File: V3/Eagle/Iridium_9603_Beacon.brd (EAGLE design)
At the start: 50.8 x 71.1 mm, 64 parts, among them J1 SS4-10-3.50-X-D, Q1 DMG3415U-7, U1 MCP111T-195I/TT, U2 SPX3819-3.3, U3 LTC3225EDDB#TRMPBF, U4 MPL3115A2LGA8, U5 ATSAMD21G18_QFN, U6 SAM-M8Q, X1 32.768

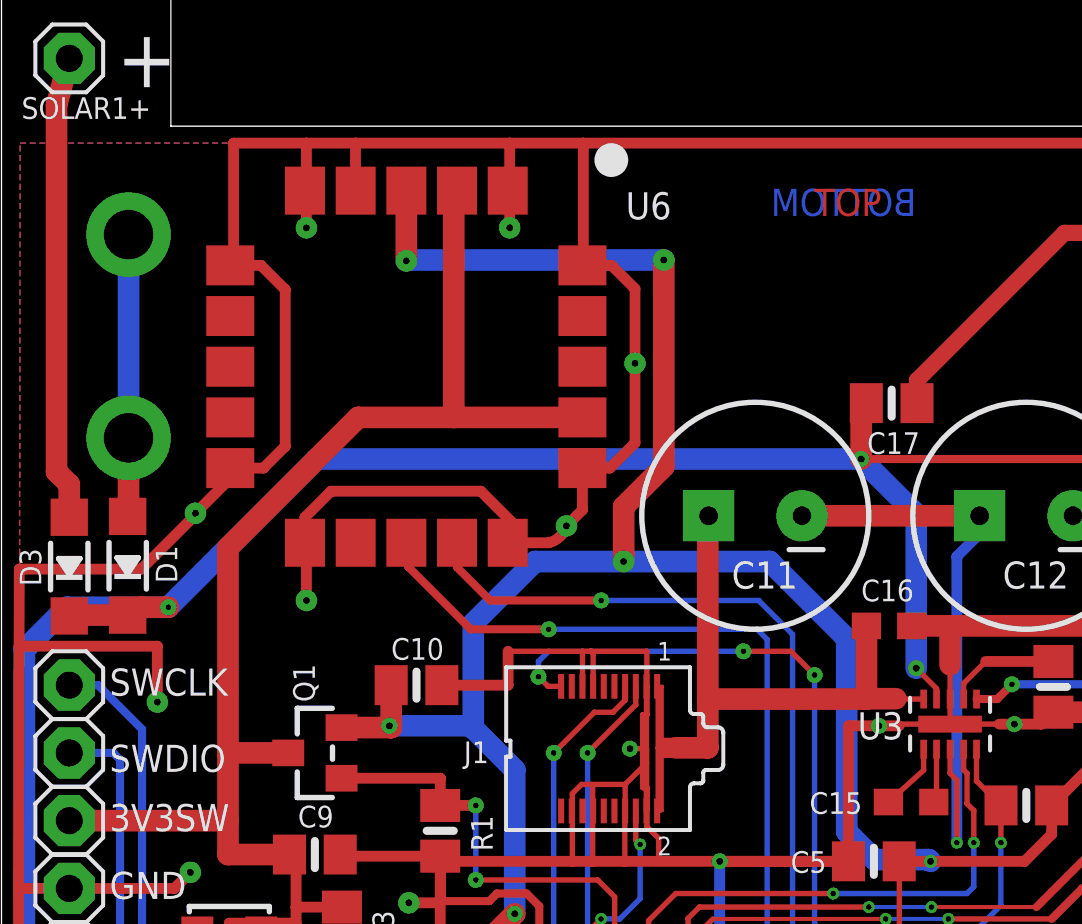
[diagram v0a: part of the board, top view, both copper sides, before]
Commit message: Improved the ground plane under the SAM-M8Q
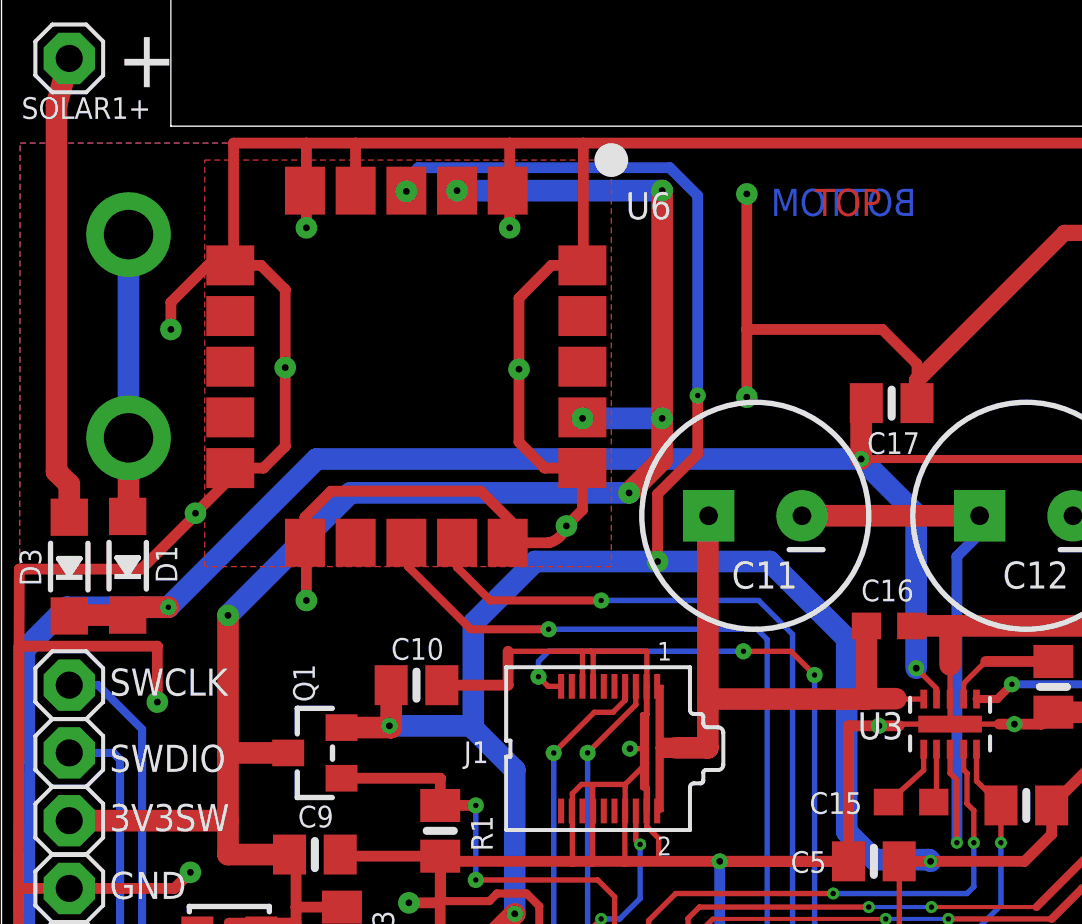
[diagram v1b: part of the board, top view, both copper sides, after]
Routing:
- net GND: track 606.7 -> 627.1 mm, vias 18 -> 22
- net 3V3SW: track 58.0 -> 71.1 mm, vias 0 -> 6
- net +3V3: track 174.7 -> 176.8 mm
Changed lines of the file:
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@@
 <text x="30.48" y="62.6745" size="1.016" layer="1" font="vector" ratio="16">TOP</text>
 <text x="34.29" y="62.6745" size="1.016" layer="16" font="vector" ratio="16" rot="MR0">BOTTOM</text>
-<text x="25.3365" y="55.4355" size="1.4224" layer="22" ratio="18" rot="MR0" align="bottom-center">Please return to:
+<text x="25.62225" y="57.24525" size="1.4224" layer="22" ratio="18" rot="MR0" align="bottom-center">Please return to:
 Durham University
 ph-cfai-bit@durham.ac.uk</text>
@@
 <vertex x="50.2285" y="5.715"/>
 </polygon>
-<polygon width="0.4064" layer="1" spacing="0.8128" pour="hatch" isolate="0.4064">
+<polygon width="0.4064" layer="1" spacing="0.8128" pour="hatch" isolate="0.4064" rank="2">
 <vertex x="0.635" y="5.715"/>
 <vertex x="0.6985" y="65.405"/>
@@
 <wire x1="21.7765" y1="60.823" x2="21.81225" y2="60.85875" width="0.4064" layer="1"/>
 <wire x1="21.81225" y1="60.85875" x2="21.81225" y2="65.405" width="0.4064" layer="1"/>
-<wire x1="21.7765" y1="53.223" x2="22.8065" y2="53.223" width="0.4064" layer="1"/>
-<wire x1="22.8065" y1="53.223" x2="23.749" y2="54.1655" width="0.4064" layer="1"/>
-<wire x1="23.749" y1="59.944" x2="22.87" y2="60.823" width="0.4064" layer="1"/>
-<wire x1="22.87" y1="60.823" x2="21.7765" y2="60.823" width="0.4064" layer="1"/>
+<wire x1="21.7765" y1="53.223" x2="20.36175" y2="53.223" width="0.4064" layer="1"/>
+<wire x1="20.36175" y1="53.223" x2="19.39925" y2="54.19725" width="0.4064" layer="1"/>
+<wire x1="19.39925" y1="59.59475" x2="20.61575" y2="60.823" width="0.4064" layer="1"/>
+<wire x1="20.61575" y1="60.823" x2="21.7765" y2="60.823" width="0.4064" layer="1"/>
 <wire x1="18.9765" y1="50.423" x2="19.4945" y2="50.423" width="0.4064" layer="1"/>
 <wire x1="19.4945" y1="50.423" x2="20.5145" y2="50.423" width="0.4064" layer="1"/>
@@
 <wire x1="7.08025" y1="38.06825" x2="6.477" y2="37.465" width="0.4064" layer="1"/>
 <wire x1="6.477" y1="37.465" x2="2.54" y2="37.465" width="0.4064" layer="1"/>
-<via x="23.749" y="57.15" extent="1-16" drill="0.254" diameter="0.8128"/>
+<via x="19.39925" y="56.92775" extent="1-16" drill="0.254" diameter="0.8128"/>
 <via x="21.17725" y="51.054" extent="1-16" drill="0.254" diameter="0.8128"/>
 <via x="19.33575" y="21.9075" extent="1-16" drill="0.254" diameter="0.8128"/>
 <wire x1="20.5145" y1="50.423" x2="21.17725" y2="51.054" width="0.4064" layer="1" curve="60"/>
 <wire x1="21.7765" y1="51.65325" x2="21.17725" y2="51.054" width="0.4064" layer="1"/>
-<wire x1="23.749" y1="54.1655" x2="23.749" y2="57.15" width="0.4064" layer="1"/>
-<wire x1="23.749" y1="59.944" x2="23.749" y2="57.15" width="0.4064" layer="1"/>
+<wire x1="19.39925" y1="54.19725" x2="19.39925" y2="56.92775" width="0.4064" layer="1"/>
+<wire x1="19.39925" y1="59.59475" x2="19.39925" y2="56.92775" width="0.4064" layer="1"/>
 <via x="7.27075" y="51.53025" extent="1-16" drill="0.254" diameter="0.8128"/>
 <wire x1="7.27075" y1="51.53025" x2="8.5765" y2="52.836" width="0.4064" layer="1"/>
@@
 <wire x1="39.850059375" y1="62.0395" x2="34.31925" y2="56.508690625" width="0.6096" layer="1"/>
 <wire x1="34.31925" y1="56.508690625" x2="34.31925" y2="55.65775" width="0.6096" layer="1"/>
+<via x="10.63625" y="56.99125" extent="1-16" drill="0.254" diameter="0.8128"/>
+<polygon width="0.4064" layer="1" isolate="0.254">
+<vertex x="7.62" y="64.77"/>
+<vertex x="22.86" y="64.77"/>
+<vertex x="22.86" y="49.53"/>
+<vertex x="7.62" y="49.53"/>
+</polygon>
+<via x="27.94" y="55.88" extent="1-16" drill="0.254" diameter="0.8128"/>
+<via x="27.94" y="63.5" extent="1-16" drill="0.254" diameter="0.8128"/>
+<wire x1="27.94" y1="63.5" x2="27.94" y2="58.42" width="0.4064" layer="1"/>
+<wire x1="27.94" y1="58.42" x2="27.94" y2="55.88" width="0.4064" layer="1"/>
+<wire x1="34.31925" y1="55.65775" x2="34.31925" y2="57.12075" width="0.4064" layer="1"/>
+<wire x1="34.31925" y1="57.12075" x2="33.02" y2="58.42" width="0.4064" layer="1"/>
+<wire x1="33.02" y1="58.42" x2="27.94" y2="58.42" width="0.4064" layer="1"/>
+<via x="6.35" y="58.42" extent="1-16" drill="0.254" diameter="0.8128"/>
+<wire x1="8.5765" y1="60.823" x2="7.737" y2="60.823" width="0.4064" layer="1"/>
+<wire x1="7.737" y1="60.823" x2="6.35" y2="59.436" width="0.4064" layer="1"/>
+<wire x1="6.35" y1="59.436" x2="6.35" y2="58.42" width="0.4064" layer="1"/>
 </signal>
 <signal name="VBAT">
@@
 <wire x1="17.68475" y1="43.52925" x2="17.68475" y2="47.40275" width="0.8128" layer="16"/>
 <wire x1="17.68475" y1="47.40275" x2="20.0025" y2="49.7205" width="0.8128" layer="16"/>
-<wire x1="20.0025" y1="49.7205" x2="23.3236" y2="49.7205" width="0.8128" layer="16"/>
-<wire x1="23.3236" y1="49.7205" x2="28.79725" y2="49.7205" width="0.8128" layer="16"/>
+<wire x1="20.0025" y1="49.7205" x2="24.5936" y2="49.7205" width="0.8128" layer="16"/>
+<wire x1="24.5936" y1="49.7205" x2="28.79725" y2="49.7205" width="0.8128" layer="16"/>
 <wire x1="28.79725" y1="49.7205" x2="31.6865" y2="46.83125" width="0.8128" layer="16"/>
 <wire x1="31.6865" y1="46.83125" x2="31.6865" y2="39.59225" width="0.8128" layer="16"/>
@@
 <wire x1="21.36775" y1="23.71725" x2="23.2156" y2="21.8694" width="0.4064" layer="1"/>
 <wire x1="23.2156" y1="21.8694" x2="27.051" y2="21.8694" width="0.4064" layer="1"/>
-<via x="23.3236" y="49.7205" extent="1-16" drill="0.254" diameter="0.8128"/>
-<wire x1="23.3236" y1="49.7205" x2="23.3236" y2="51.7716" width="0.8128" layer="1"/>
-<wire x1="23.3236" y1="51.7716" x2="24.8285" y2="53.2765" width="0.8128" layer="1"/>
-<wire x1="24.8285" y1="53.2765" x2="24.8285" y2="61.0235" width="0.8128" layer="1"/>
-<via x="24.8285" y="61.0235" extent="1-16" drill="0.254" diameter="0.8128"/>
-<wire x1="24.8285" y1="61.0235" x2="15.20825" y2="61.0235" width="0.8128" layer="16"/>
-<wire x1="15.20825" y1="61.0235" x2="15.1765" y2="60.99175" width="0.8128" layer="16"/>
-<via x="15.1765" y="60.99175" extent="1-16" drill="0.254" diameter="0.8128"/>
-<wire x1="15.1765" y1="60.99175" x2="15.1765" y2="63.623" width="0.8128" layer="1"/>
+<via x="24.5936" y="49.7205" extent="1-16" drill="0.254" diameter="0.8128"/>
+<wire x1="24.5936" y1="49.7205" x2="24.5936" y2="52.24785" width="0.4064" layer="1"/>
+<wire x1="24.5936" y1="52.24785" x2="26.0985" y2="53.75275" width="0.4064" layer="1"/>
+<wire x1="26.0985" y1="53.75275" x2="26.0985" y2="55.9435" width="0.4064" layer="1"/>
+<via x="26.0985" y="55.9435" extent="1-16" drill="0.2032" diameter="0.6096"/>
+<wire x1="26.0985" y1="55.9435" x2="26.0985" y2="63.4365" width="0.4064" layer="16"/>
+<wire x1="26.0985" y1="63.4365" x2="25.05075" y2="64.48425" width="0.4064" layer="16"/>
+<wire x1="25.05075" y1="64.48425" x2="15.621" y2="64.48425" width="0.4064" layer="16"/>
+<wire x1="15.621" y1="64.48425" x2="15.1765" y2="64.03975" width="0.4064" layer="16"/>
+<wire x1="15.1765" y1="64.03975" x2="15.1765" y2="63.59525" width="0.4064" layer="16"/>
+<via x="15.1765" y="63.59525" extent="1-16" drill="0.254" diameter="0.8128"/>
+<wire x1="15.1765" y1="63.59525" x2="15.1765" y2="63.623" width="0.4064" layer="1"/>
 </signal>
 <signal name="N$2">
@@
 <contactref element="U6" pad="17"/>
 <contactref element="U6" pad="2"/>
-<wire x1="8.49" y1="42.545" x2="8.49" y2="50.24125" width="0.8128" layer="1"/>
-<wire x1="8.49" y1="50.24125" x2="13.37175" y2="55.123" width="0.8128" layer="1"/>
-<wire x1="13.37175" y1="55.123" x2="16.9545" y2="55.123" width="0.8128" layer="1"/>
-<wire x1="16.9545" y1="55.123" x2="21.7765" y2="55.123" width="0.8128" layer="1"/>
-<wire x1="17.0765" y1="63.623" x2="16.9545" y2="63.623" width="0.8128" layer="1"/>
-<wire x1="16.9545" y1="63.623" x2="16.9545" y2="55.123" width="0.8128" layer="1"/>
+<wire x1="8.49" y1="42.545" x2="8.49" y2="47.70125" width="0.8128" layer="1"/>
+<via x="8.49" y="47.70125" extent="1-16" drill="0.254" diameter="0.8128"/>
+<wire x1="8.49" y1="47.70125" x2="13.081" y2="52.29225" width="0.8128" layer="16"/>
+<wire x1="13.081" y1="52.29225" x2="23.52675" y2="52.29225" width="0.8128" layer="16"/>
+<via x="23.52675" y="52.29225" extent="1-16" drill="0.254" diameter="0.8128"/>
+<wire x1="23.52675" y1="52.29225" x2="24.765" y2="53.5305" width="0.8128" layer="1"/>
+<wire x1="24.765" y1="53.5305" x2="24.765" y2="55.08625" width="0.8128" layer="1"/>
+<via x="24.765" y="63.627" extent="1-16" drill="0.254" diameter="0.8128"/>
+<wire x1="24.765" y1="55.08625" x2="24.765" y2="63.627" width="0.8128" layer="1"/>
+<wire x1="24.765" y1="63.627" x2="24.761" y2="63.623" width="0.8128" layer="16"/>
+<wire x1="24.761" y1="63.623" x2="17.0765" y2="63.623" width="0.8128" layer="16"/>
+<wire x1="21.7805" y1="55.08625" x2="24.765" y2="55.08625" width="0.8128" layer="16"/>
+<via x="24.765" y="55.08625" extent="1-16" drill="0.254" diameter="0.8128"/>
+<wire x1="17.0765" y1="63.623" x2="17.04975" y2="63.59625" width="0.8128" layer="1"/>
+<via x="17.0765" y="63.623" extent="1-16" drill="0.254" diameter="0.8128"/>
+<via x="21.7805" y="55.08625" extent="1-16" drill="0.254" diameter="0.8128"/>
+<wire x1="21.7805" y1="55.08625" x2="21.7765" y2="55.123" width="0.8128" layer="1"/>
 </signal>
 <signal name="LTC3225_VOUT">

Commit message: Final tweaks before sending V3 for manufacture
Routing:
- net GND: track 627.1 -> 633.8 mm, vias 22 -> 26
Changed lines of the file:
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@@
 <wire x1="8.5765" y1="53.223" x2="9.82075" y2="53.223" width="0.4064" layer="1"/>
 <wire x1="9.82075" y1="53.223" x2="10.63625" y2="54.0385" width="0.4064" layer="1"/>
-<wire x1="10.63625" y1="54.0385" x2="10.63625" y2="59.91225" width="0.4064" layer="1"/>
+<wire x1="10.63625" y1="54.0385" x2="10.63625" y2="54.61" width="0.4064" layer="1"/>
+<wire x1="10.63625" y1="54.61" x2="10.63625" y2="56.99125" width="0.4064" layer="1"/>
+<wire x1="10.63625" y1="56.99125" x2="10.63625" y2="59.69" width="0.4064" layer="1"/>
+<wire x1="10.63625" y1="59.69" x2="10.63625" y2="59.91225" width="0.4064" layer="1"/>
 <wire x1="10.63625" y1="59.91225" x2="9.7255" y2="60.823" width="0.4064" layer="1"/>
 <wire x1="9.7255" y1="60.823" x2="8.5765" y2="60.823" width="0.4064" layer="1"/>
@@
 <wire x1="20.5145" y1="50.423" x2="21.17725" y2="51.054" width="0.4064" layer="1" curve="60"/>
 <wire x1="21.7765" y1="51.65325" x2="21.17725" y2="51.054" width="0.4064" layer="1"/>
-<wire x1="19.39925" y1="54.19725" x2="19.39925" y2="56.92775" width="0.4064" layer="1"/>
+<wire x1="19.39925" y1="54.19725" x2="19.39925" y2="54.61" width="0.4064" layer="1"/>
+<wire x1="19.39925" y1="54.61" x2="19.39925" y2="56.92775" width="0.4064" layer="1"/>
 <wire x1="19.39925" y1="59.59475" x2="19.39925" y2="56.92775" width="0.4064" layer="1"/>
 <via x="7.27075" y="51.53025" extent="1-16" drill="0.254" diameter="0.8128"/>
@@
 <via x="10.63625" y="56.99125" extent="1-16" drill="0.254" diameter="0.8128"/>
 <polygon width="0.4064" layer="1" isolate="0.254">
-<vertex x="7.62" y="64.77"/>
-<vertex x="22.86" y="64.77"/>
-<vertex x="22.86" y="49.53"/>
-<vertex x="7.62" y="49.53"/>
+<vertex x="6.88975" y="65.37325"/>
+<vertex x="23.78075" y="65.37325"/>
+<vertex x="23.78075" y="49.022"/>
+<vertex x="6.88975" y="49.022"/>
 </polygon>
 <via x="27.94" y="55.88" extent="1-16" drill="0.254" diameter="0.8128"/>
@@
 <wire x1="34.31925" y1="57.12075" x2="33.02" y2="58.42" width="0.4064" layer="1"/>
 <wire x1="33.02" y1="58.42" x2="27.94" y2="58.42" width="0.4064" layer="1"/>
-<via x="6.35" y="58.42" extent="1-16" drill="0.254" diameter="0.8128"/>
 <wire x1="8.5765" y1="60.823" x2="7.737" y2="60.823" width="0.4064" layer="1"/>
-<wire x1="7.737" y1="60.823" x2="6.35" y2="59.436" width="0.4064" layer="1"/>
-<wire x1="6.35" y1="59.436" x2="6.35" y2="58.42" width="0.4064" layer="1"/>
+<via x="12.7" y="59.69" extent="1-16" drill="0.254" diameter="0.8128"/>
+<via x="19.05" y="59.69" extent="1-16" drill="0.254" diameter="0.8128"/>
+<via x="15.24" y="57.15" extent="1-16" drill="0.254" diameter="0.8128"/>
+<via x="12.7" y="54.61" extent="1-16" drill="0.254" diameter="0.8128"/>
+<via x="19.05" y="54.61" extent="1-16" drill="0.254" diameter="0.8128"/>
+<wire x1="19.05" y1="54.61" x2="19.39925" y2="54.61" width="0.4064" layer="1"/>
+<wire x1="12.7" y1="54.61" x2="10.63625" y2="54.61" width="0.4064" layer="1"/>
+<wire x1="12.7" y1="59.69" x2="10.63625" y2="59.69" width="0.4064" layer="1"/>
+<wire x1="19.05" y1="59.69" x2="19.39925" y2="59.69" width="0.4064" layer="1"/>
+<wire x1="19.39925" y1="59.69" x2="19.39925" y2="59.59475" width="0.4064" layer="1"/>
+<wire x1="15.24" y1="57.15" x2="10.63625" y2="57.15" width="0.4064" layer="1"/>
+<wire x1="10.63625" y1="57.15" x2="10.63625" y2="56.99125" width="0.4064" layer="1"/>
 </signal>
 <signal name="VBAT">
@@
 <wire x1="24.5936" y1="52.24785" x2="26.0985" y2="53.75275" width="0.4064" layer="1"/>
 <wire x1="26.0985" y1="53.75275" x2="26.0985" y2="55.9435" width="0.4064" layer="1"/>
-<via x="26.0985" y="55.9435" extent="1-16" drill="0.2032" diameter="0.6096"/>
+<via x="26.0985" y="55.9435" extent="1-16" drill="0.254" diameter="0.6096"/>
 <wire x1="26.0985" y1="55.9435" x2="26.0985" y2="63.4365" width="0.4064" layer="16"/>
 <wire x1="26.0985" y1="63.4365" x2="25.05075" y2="64.48425" width="0.4064" layer="16"/>
@@
 <wire x1="13.081" y1="52.29225" x2="23.52675" y2="52.29225" width="0.8128" layer="16"/>
 <via x="23.52675" y="52.29225" extent="1-16" drill="0.254" diameter="0.8128"/>
-<wire x1="23.52675" y1="52.29225" x2="24.765" y2="53.5305" width="0.8128" layer="1"/>
-<wire x1="24.765" y1="53.5305" x2="24.765" y2="55.08625" width="0.8128" layer="1"/>
+<wire x1="23.52675" y1="52.29225" x2="24.765" y2="53.5305" width="0.6096" layer="1"/>
+<wire x1="24.765" y1="53.5305" x2="24.765" y2="55.08625" width="0.6096" layer="1"/>
 <via x="24.765" y="63.627" extent="1-16" drill="0.254" diameter="0.8128"/>
-<wire x1="24.765" y1="55.08625" x2="24.765" y2="63.627" width="0.8128" layer="1"/>
+<wire x1="24.765" y1="55.08625" x2="24.765" y2="63.627" width="0.6096" layer="1"/>
 <wire x1="24.765" y1="63.627" x2="24.761" y2="63.623" width="0.8128" layer="16"/>
-<wire x1="24.761" y1="63.623" x2="17.0765" y2="63.623" width="0.8128" layer="16"/>
+<wire x1="24.761" y1="63.623" x2="17.0765" y2="63.623" width="0.6096" layer="16"/>
 <wire x1="21.7805" y1="55.08625" x2="24.765" y2="55.08625" width="0.8128" layer="16"/>
 <via x="24.765" y="55.08625" extent="1-16" drill="0.254" diameter="0.8128"/>
@@
 <wire x1="36.5506" y1="44.5643" x2="37.3253" y2="44.5643" width="0.3048" layer="1"/>
 <wire x1="37.3253" y1="44.5643" x2="37.87775" y2="45.11675" width="0.3048" layer="1"/>
-<via x="37.87775" y="45.11675" extent="1-16" drill="0.2032" diameter="0.6096"/>
+<via x="37.87775" y="45.11675" extent="1-16" drill="0.254" diameter="0.6096"/>
 <wire x1="37.87775" y1="45.11675" x2="43.14825" y2="45.11675" width="0.3048" layer="16"/>
-<via x="43.14825" y="45.11675" extent="1-16" drill="0.2032" diameter="0.6096"/>
+<via x="43.14825" y="45.11675" extent="1-16" drill="0.254" diameter="0.6096"/>
 <wire x1="43.14825" y1="45.11675" x2="45.72" y2="47.6885" width="0.3048" layer="1"/>
 <wire x1="45.72" y1="47.6885" x2="45.72" y2="49.53" width="0.3048" layer="1"/>
